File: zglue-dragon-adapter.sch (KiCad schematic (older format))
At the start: 56 parts, among them J1 543630489, J2 543630489, U1 zGlue-Dragon

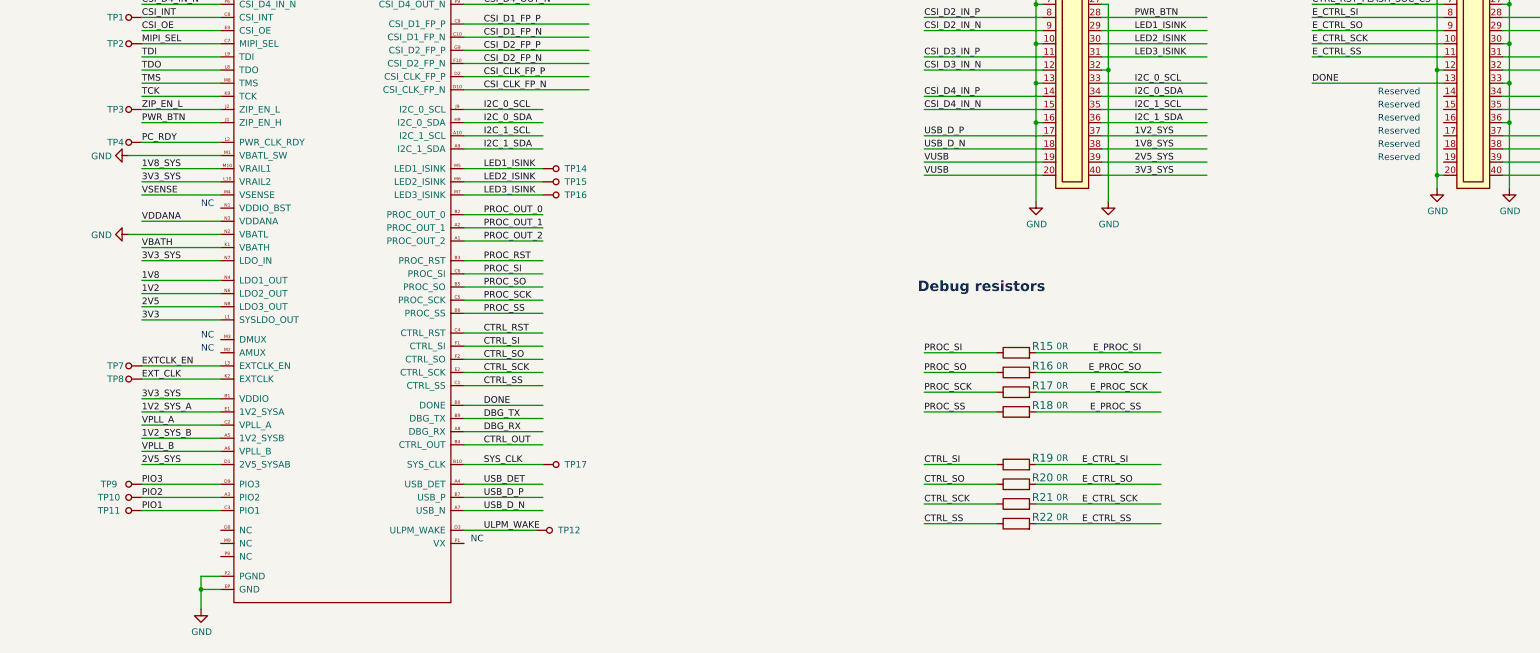
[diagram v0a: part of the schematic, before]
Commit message: Layout polishing, connected PROC_RST and CTRL_RST to chip via 0R
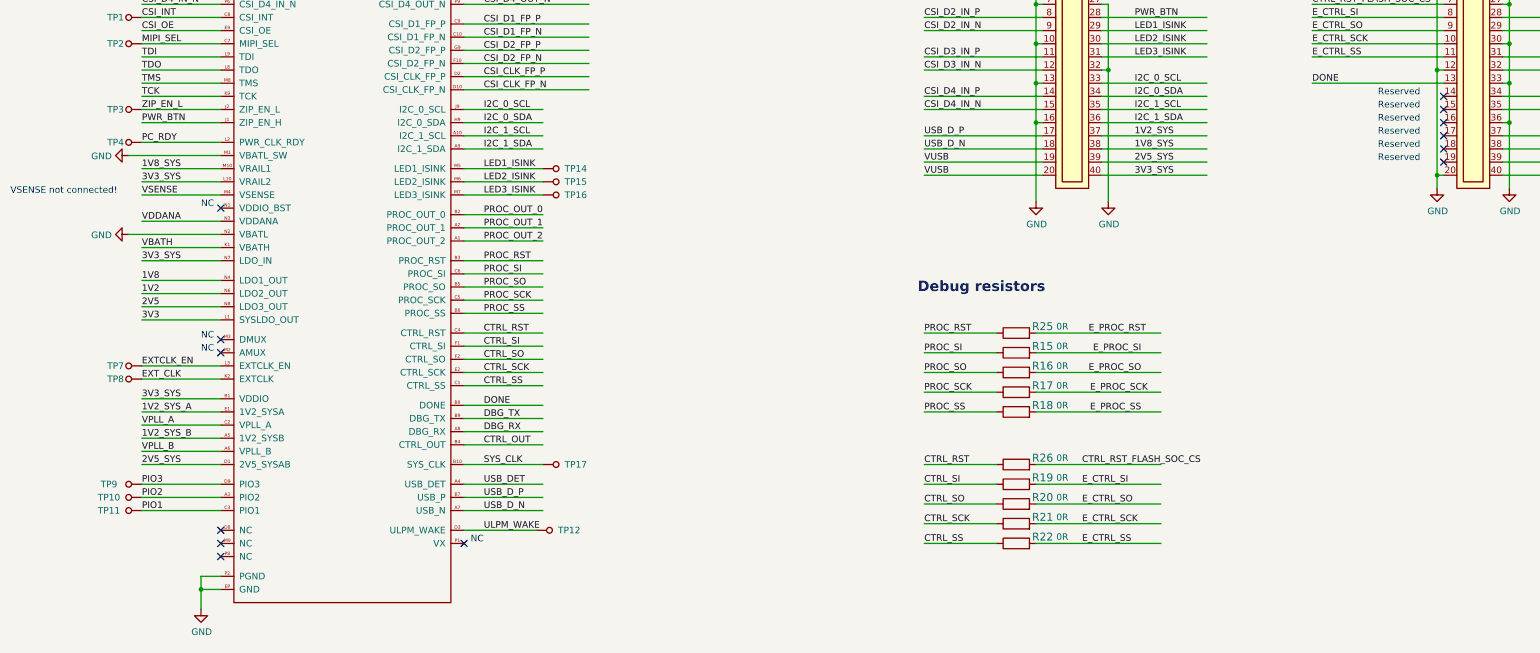
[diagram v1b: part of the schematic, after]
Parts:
- added R25, R26: R_0R_0402, antmicro-footprints:0402-res, symbol antmicroResistors0402:R_0R_0402
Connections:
- wire segments 259 -> 263
- no-connect marks 0 -> 13
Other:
- note added: "VSENSE not connected!"
- moved on the sheet: R19, R20, R21, R22
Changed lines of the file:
@@
 Text Label 10850 2150 0    50   ~ 0
 CTRL_RST_FLASH_SOC_CS
-Text Label 7900 5650 0    50   ~ 0
+Text Label 7900 5800 0    50   ~ 0
 CTRL_SI
-Text Label 7900 5800 0    50   ~ 0
+Text Label 7900 5950 0    50   ~ 0
 CTRL_SO
-Text Label 7900 5950 0    50   ~ 0
+Text Label 7900 6100 0    50   ~ 0
 CTRL_SCK
-Text Label 7900 6100 0    50   ~ 0
+Text Label 7900 6250 0    50   ~ 0
 CTRL_SS
 Text Label 9500 2050 0    50   ~ 0
@@
 L antmicroResistors0402:R_0R_0402 R19
 U 1 1 5E57F379
-P 8600 5650
-F 0 "R19" H 8800 5700 60  0000 C CNN
-F 1 "R_0R_0402" H 8600 5500 60  0001 C CNN
-F 2 "antmicro-footprints:0402-res" H 8800 5850 60  0001 L CNN
-F 3 "" H 8600 5650 50  0001 C CNN
-F 4 "PANASONIC" H 8800 6050 60  0001 L CNN "Manufacturer"
-F 5 "ERJ2GE0R00X" H 8800 5950 60  0001 L CNN "MPN"
-F 6 "0R" H 8950 5700 50  0000 C CNN "Val"
-	1    8600 5650
-	1    0    0    -1
-$EndComp
-Wire Wire Line
-	7900 5650 8450 5650
-$Comp
-L antmicroResistors0402:R_0R_0402 R20
-U 1 1 5E57F389
 P 8600 5800
-F 0 "R20" H 8800 5850 60  0000 C CNN
+F 0 "R19" H 8800 5850 60  0000 C CNN
 F 1 "R_0R_0402" H 8600 5650 60  0001 C CNN
 F 2 "antmicro-footprints:0402-res" H 8800 6000 60  0001 L CNN
@@
 	7900 5800 8450 5800
 $Comp
-L antmicroResistors0402:R_0R_0402 R21
-U 1 1 5E57F395
+L antmicroResistors0402:R_0R_0402 R20
+U 1 1 5E57F389
 P 8600 5950
-F 0 "R21" H 8800 6000 60  0000 C CNN
+F 0 "R20" H 8800 6000 60  0000 C CNN
 F 1 "R_0R_0402" H 8600 5800 60  0001 C CNN
 F 2 "antmicro-footprints:0402-res" H 8800 6150 60  0001 L CNN
@@
 	7900 5950 8450 5950
 $Comp
-L antmicroResistors0402:R_0R_0402 R22
-U 1 1 5E57F3A1
+L antmicroResistors0402:R_0R_0402 R21
+U 1 1 5E57F395
 P 8600 6100
-F 0 "R22" H 8800 6150 60  0000 C CNN
+F 0 "R21" H 8800 6150 60  0000 C CNN
 F 1 "R_0R_0402" H 8600 5950 60  0001 C CNN
 F 2 "antmicro-footprints:0402-res" H 8800 6300 60  0001 L CNN
@@
 Wire Wire Line
 	7900 6100 8450 6100
+$Comp
+L antmicroResistors0402:R_0R_0402 R22
+U 1 1 5E57F3A1
+P 8600 6250
+F 0 "R22" H 8800 6300 60  0000 C CNN
+F 1 "R_0R_0402" H 8600 6100 60  0001 C CNN
+F 2 "antmicro-footprints:0402-res" H 8800 6450 60  0001 L CNN
+F 3 "" H 8600 6250 50  0001 C CNN
+F 4 "PANASONIC" H 8800 6650 60  0001 L CNN "Manufacturer"
+F 5 "ERJ2GE0R00X" H 8800 6550 60  0001 L CNN "MPN"
+F 6 "0R" H 8950 6300 50  0000 C CNN "Val"
+	1    8600 6250
+	1    0    0    -1
+$EndComp
+Wire Wire Line
+	7900 6250 8450 6250
 Text Notes 7850 4350 0    79   ~ 16
 Debug resistors
@@
 Text Label 9550 5250 2    50   ~ 0
 E_PROC_SS
-Text Label 9100 5650 0    50   ~ 0
+Text Label 9100 5800 0    50   ~ 0
 E_CTRL_SI
-Text Label 9100 5800 0    50   ~ 0
+Text Label 9100 5950 0    50   ~ 0
 E_CTRL_SO
-Text Label 9100 5950 0    50   ~ 0
+Text Label 9100 6100 0    50   ~ 0
 E_CTRL_SCK
-Text Label 9100 6100 0    50   ~ 0
+Text Label 9100 6250 0    50   ~ 0
 E_CTRL_SS
 Wire Wire Line
@@
 	8750 5250 9700 5250
 Wire Wire Line
-	8750 5650 9700 5650
-Wire Wire Line
 	8750 5800 9700 5800
 Wire Wire Line
@@
 Wire Wire Line
 	8750 6100 9700 6100
+Wire Wire Line
+	8750 6250 9700 6250
 Text Label 1950 2450 0    50   ~ 0
 MIPI_SEL
@@
 Wire Wire Line
 	10900 8250 11650 8250
+NoConn ~ 2550 3700
+NoConn ~ 2550 4700
+NoConn ~ 2550 4800
+NoConn ~ 4400 6250
+NoConn ~ 11850 2850
+NoConn ~ 11850 2950
+NoConn ~ 11850 3050
+NoConn ~ 11850 3150
+NoConn ~ 11850 3250
+NoConn ~ 11850 3350
+NoConn ~ 2550 6150
+NoConn ~ 2550 6250
+NoConn ~ 2550 6350
+$Comp
+L antmicroResistors0402:R_0R_0402 R25
+U 1 1 5DC78E2D
+P 8600 4650
+F 0 "R25" H 8800 4700 60  0000 C CNN
+F 1 "R_0R_0402" H 8600 4500 60  0001 C CNN
+F 2 "antmicro-footprints:0402-res" H 8800 4850 60  0001 L CNN
+F 3 "" H 8600 4650 50  0001 C CNN
+F 4 "PANASONIC" H 8800 5050 60  0001 L CNN "Manufacturer"
+F 5 "ERJ2GE0R00X" H 8800 4950 60  0001 L CNN "MPN"
+F 6 "0R" H 8950 4700 50  0000 C CNN "Val"
+	1    8600 4650
+	1    0    0    -1
+$EndComp
+Wire Wire Line
+	8450 4650 7900 4650
+Wire Wire Line
+	8750 4650 9700 4650
+Text Label 7900 4650 0    50   ~ 0
+PROC_RST
+Text Label 9150 4650 0    50   ~ 0
+E_PROC_RST
+$Comp
+L antmicroResistors0402:R_0R_0402 R26
+U 1 1 5DCC1CB8
+P 8600 5650
+F 0 "R26" H 8800 5700 60  0000 C CNN
+F 1 "R_0R_0402" H 8600 5500 60  0001 C CNN
+F 2 "antmicro-footprints:0402-res" H 8800 5850 60  0001 L CNN
+F 3 "" H 8600 5650 50  0001 C CNN
+F 4 "PANASONIC" H 8800 6050 60  0001 L CNN "Manufacturer"
+F 5 "ERJ2GE0R00X" H 8800 5950 60  0001 L CNN "MPN"
+F 6 "0R" H 8950 5700 50  0000 C CNN "Val"
+	1    8600 5650
+	1    0    0    -1
+$EndComp
+Wire Wire Line
+	8450 5650 7900 5650
+Wire Wire Line
+	8750 5650 9700 5650
+Text Label 9100 5650 0    50   ~ 0
+CTRL_RST_FLASH_SOC_CS
+Text Label 7900 5650 0    50   ~ 0
+CTRL_RST
+Text Notes 950  3600 0    50   ~ 0
+VSENSE not connected!
 $EndSCHEMATC

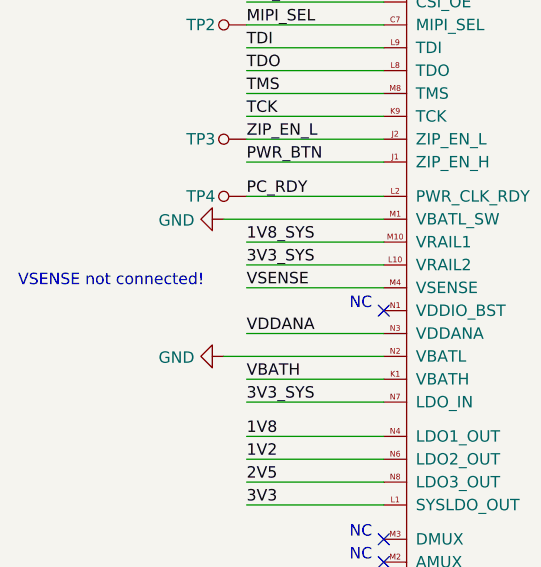
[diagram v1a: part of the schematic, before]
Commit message: Added testpad for VSENSE
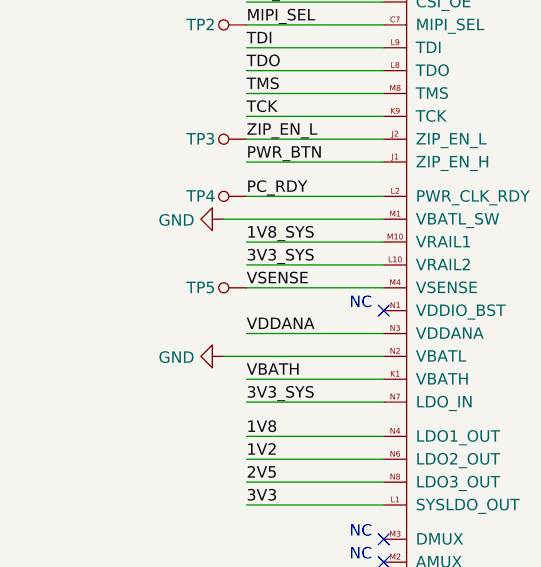
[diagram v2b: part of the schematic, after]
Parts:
- added TP5: TP_SMD1MM, antmicro-footprints:Testpoint_smd_1mm, symbol antmicroTestPoints:TP_SMD1MM
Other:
- note removed: "VSENSE not connected!"
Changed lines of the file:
@@
 Text Label 7900 5650 0    50   ~ 0
 CTRL_RST
-Text Notes 950  3600 0    50   ~ 0
-VSENSE not connected!
+$Comp
+L antmicroTestPoints:TP_SMD1MM TP5
+U 1 1 5DB1BFE4
+P 1850 3600
+F 0 "TP5" V 1850 3500 50  0000 C CNN
+F 1 "TP_SMD1MM" H 1850 3500 50  0001 C CNN
+F 2 "antmicro-footprints:Testpoint_smd_1mm" H 2050 3800 60  0001 L CNN
+F 3 "" H 2050 3900 60  0001 L CNN
+	1    1850 3600
+	0    1    1    0
+$EndComp
 $EndSCHEMATC

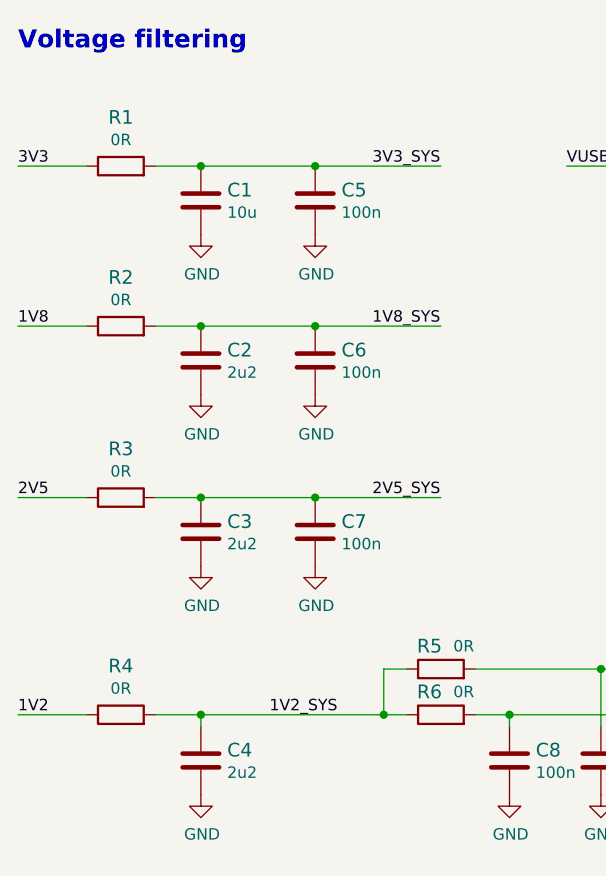
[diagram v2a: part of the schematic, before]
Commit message: Moved C1,2,3,4 closer to LDO output pins
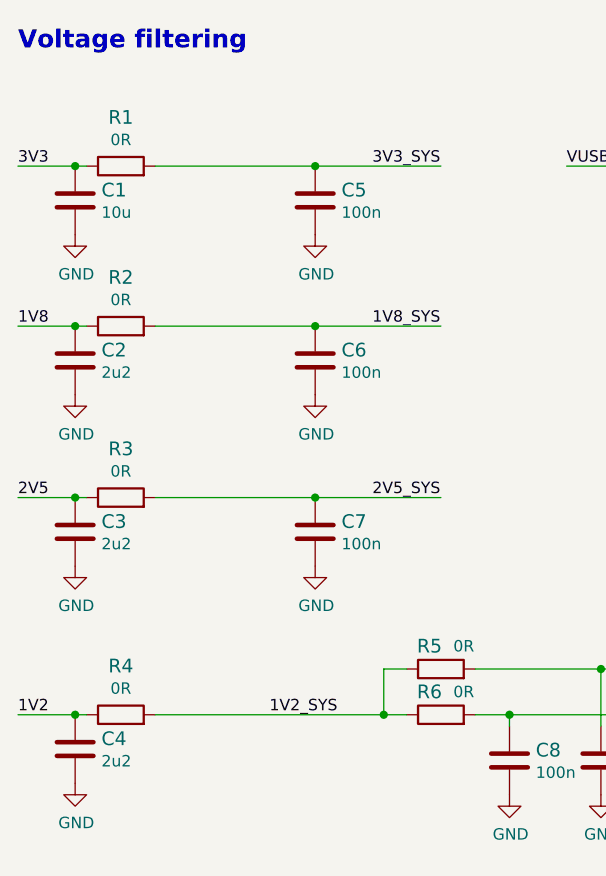
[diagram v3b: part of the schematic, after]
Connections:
- wire segments 263 -> 262
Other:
- moved on the sheet: C1, C2, C3, C4
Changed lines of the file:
@@
 L antmicroCapacitors0402:C_10u_0402 C1
 U 1 1 5DA0000B
-P 2000 8200
-F 0 "C1" H 2115 8245 60  0000 L CNN
-F 1 "C_10u_0402" H 2000 8050 60  0001 C CNN
-F 2 "antmicro-footprints:0402-cap" H 2200 8400 60  0001 L CNN
-F 3 "" H 2000 8200 50  0001 C CNN
-F 4 "TDK" H 2200 8600 60  0001 L CNN "Manufacturer"
-F 5 "C1005X5R0J106M050BC" H 2200 8500 60  0001 L CNN "MPN"
-F 6 "10u" H 2115 8147 50  0000 L CNN "Val"
-	1    2000 8200
+P 1450 8200
+F 0 "C1" H 1565 8245 60  0000 L CNN
+F 1 "C_10u_0402" H 1450 8050 60  0001 C CNN
+F 2 "antmicro-footprints:0402-cap" H 1650 8400 60  0001 L CNN
+F 3 "" H 1450 8200 50  0001 C CNN
+F 4 "TDK" H 1650 8600 60  0001 L CNN "Manufacturer"
+F 5 "C1005X5R0J106M050BC" H 1650 8500 60  0001 L CNN "MPN"
+F 6 "10u" H 1565 8147 50  0000 L CNN "Val"
+	1    1450 8200
 	1    0    0    -1
 $EndComp
@@
 L power:GND #PWR03
 U 1 1 5DA0044B
-P 2000 8350
-F 0 "#PWR03" H 2000 8100 50  0001 C CNN
-F 1 "GND" H 2005 8177 50  0000 C CNN
-F 2 "" H 2000 8350 50  0001 C CNN
-F 3 "" H 2000 8350 50  0001 C CNN
-	1    2000 8350
+P 1450 8350
+F 0 "#PWR03" H 1450 8100 50  0001 C CNN
+F 1 "GND" H 1455 8177 50  0000 C CNN
+F 2 "" H 1450 8350 50  0001 C CNN
+F 3 "" H 1450 8350 50  0001 C CNN
+	1    1450 8350
 	1    0    0    -1
 $EndComp
@@
 $EndComp
 Wire Wire Line
-	1800 8050 2000 8050
-Connection ~ 2000 8050
-Wire Wire Line
-	2000 8050 2500 8050
-Wire Wire Line
 	2500 8050 3050 8050
 Connection ~ 2500 8050
 Wire Wire Line
-	1500 8050 1200 8050
+	1500 8050 1450 8050
 Text Label 1200 8050 0    50   ~ 0
 3V3
@@
 L power:GND #PWR04
 U 1 1 5DA29CC6
-P 2000 9050
-F 0 "#PWR04" H 2000 8800 50  0001 C CNN
-F 1 "GND" H 2005 8877 50  0000 C CNN
-F 2 "" H 2000 9050 50  0001 C CNN
-F 3 "" H 2000 9050 50  0001 C CNN
-	1    2000 9050
+P 1450 9050
+F 0 "#PWR04" H 1450 8800 50  0001 C CNN
+F 1 "GND" H 1455 8877 50  0000 C CNN
+F 2 "" H 1450 9050 50  0001 C CNN
+F 3 "" H 1450 9050 50  0001 C CNN
+	1    1450 9050
 	1    0    0    -1
 $EndComp
@@
 Connection ~ 2500 8750
 Wire Wire Line
-	1500 8750 1200 8750
-Wire Wire Line
-	1800 8750 2000 8750
+	1500 8750 1450 8750
 $Comp
 L antmicroCapacitors0402:C_2u2_0402 C2
 U 1 1 5DA30683
-P 2000 8900
-F 0 "C2" H 2115 8945 60  0000 L CNN
-F 1 "C_2u2_0402" H 2000 8750 60  0001 C CNN
-F 2 "antmicro-footprints:0402-cap" H 2200 9100 60  0001 L CNN
-F 3 "" H 2000 8900 50  0001 C CNN
-F 4 "TDK" H 2200 9300 60  0001 L CNN "Manufacturer"
-F 5 "C1005X5R1A225K050BC" H 2200 9200 60  0001 L CNN "MPN"
-F 6 "2u2" H 2115 8847 50  0000 L CNN "Val"
-	1    2000 8900
-	1    0    0    -1
-$EndComp
-Connection ~ 2000 8750
-Wire Wire Line
-	2000 8750 2500 8750
+P 1450 8900
+F 0 "C2" H 1565 8945 60  0000 L CNN
+F 1 "C_2u2_0402" H 1450 8750 60  0001 C CNN
+F 2 "antmicro-footprints:0402-cap" H 1650 9100 60  0001 L CNN
+F 3 "" H 1450 8900 50  0001 C CNN
+F 4 "TDK" H 1650 9300 60  0001 L CNN "Manufacturer"
+F 5 "C1005X5R1A225K050BC" H 1650 9200 60  0001 L CNN "MPN"
+F 6 "2u2" H 1565 8847 50  0000 L CNN "Val"
+	1    1450 8900
+	1    0    0    -1
+$EndComp
 $Comp
 L antmicroCapacitors0402:C_100n_0402_6V3 C8
@@
 L power:GND #PWR06
 U 1 1 5DA307EF
-P 2000 10800
-F 0 "#PWR06" H 2000 10550 50  0001 C CNN
-F 1 "GND" H 2005 10627 50  0000 C CNN
-F 2 "" H 2000 10800 50  0001 C CNN
-F 3 "" H 2000 10800 50  0001 C CNN
-	1    2000 10800
+P 1450 10750
+F 0 "#PWR06" H 1450 10500 50  0001 C CNN
+F 1 "GND" H 1455 10577 50  0000 C CNN
+F 2 "" H 1450 10750 50  0001 C CNN
+F 3 "" H 1450 10750 50  0001 C CNN
+	1    1450 10750
 	1    0    0    -1
 $EndComp
@@
 $EndComp
 Wire Wire Line
-	1500 10450 1200 10450
-Wire Wire Line
-	1800 10450 2000 10450
-Connection ~ 2000 10450
+	1500 10450 1450 10450
 $Comp
 L antmicroCapacitors0402:C_2u2_0402 C4
 U 1 1 5DA3080C
-P 2000 10650
-F 0 "C4" H 2115 10695 60  0000 L CNN
-F 1 "C_2u2_0402" H 2000 10500 60  0001 C CNN
-F 2 "antmicro-footprints:0402-cap" H 2200 10850 60  0001 L CNN
-F 3 "" H 2000 10650 50  0001 C CNN
-F 4 "TDK" H 2200 11050 60  0001 L CNN "Manufacturer"
-F 5 "C1005X5R1A225K050BC" H 2200 10950 60  0001 L CNN "MPN"
-F 6 "2u2" H 2115 10597 50  0000 L CNN "Val"
-	1    2000 10650
+P 1450 10600
+F 0 "C4" H 1565 10645 60  0000 L CNN
+F 1 "C_2u2_0402" H 1450 10450 60  0001 C CNN
+F 2 "antmicro-footprints:0402-cap" H 1650 10800 60  0001 L CNN
+F 3 "" H 1450 10600 50  0001 C CNN
+F 4 "TDK" H 1650 11000 60  0001 L CNN "Manufacturer"
+F 5 "C1005X5R1A225K050BC" H 1650 10900 60  0001 L CNN "MPN"
+F 6 "2u2" H 1565 10547 50  0000 L CNN "Val"
+	1    1450 10600
 	1    0    0    -1
 $EndComp
@@
 Wire Wire Line
 	3200 10450 3350 10450
-Wire Wire Line
-	2000 10450 2800 10450
-Wire Wire Line
-	2000 10500 2000 10450
 $Comp
 L power:GND #PWR011
@@
 L power:GND #PWR05
 U 1 1 5DB84A7E
-P 2000 9800
-F 0 "#PWR05" H 2000 9550 50  0001 C CNN
-F 1 "GND" H 2005 9627 50  0000 C CNN
-F 2 "" H 2000 9800 50  0001 C CNN
-F 3 "" H 2000 9800 50  0001 C CNN
-	1    2000 9800
+P 1450 9800
+F 0 "#PWR05" H 1450 9550 50  0001 C CNN
+F 1 "GND" H 1455 9627 50  0000 C CNN
+F 2 "" H 1450 9800 50  0001 C CNN
+F 3 "" H 1450 9800 50  0001 C CNN
+	1    1450 9800
 	1    0    0    -1
 $EndComp
@@
 Connection ~ 2500 9500
 Wire Wire Line
-	1500 9500 1200 9500
-Wire Wire Line
-	1800 9500 2000 9500
+	1500 9500 1450 9500
 $Comp
 L antmicroCapacitors0402:C_2u2_0402 C3
 U 1 1 5DB84A9B
-P 2000 9650
-F 0 "C3" H 2115 9695 60  0000 L CNN
-F 1 "C_2u2_0402" H 2000 9500 60  0001 C CNN
-F 2 "antmicro-footprints:0402-cap" H 2200 9850 60  0001 L CNN
-F 3 "" H 2000 9650 50  0001 C CNN
-F 4 "TDK" H 2200 10050 60  0001 L CNN "Manufacturer"
-F 5 "C1005X5R1A225K050BC" H 2200 9950 60  0001 L CNN "MPN"
-F 6 "2u2" H 2115 9597 50  0000 L CNN "Val"
-	1    2000 9650
-	1    0    0    -1
-$EndComp
-Connection ~ 2000 9500
-Wire Wire Line
-	2000 9500 2500 9500
+P 1450 9650
+F 0 "C3" H 1565 9695 60  0000 L CNN
+F 1 "C_2u2_0402" H 1450 9500 60  0001 C CNN
+F 2 "antmicro-footprints:0402-cap" H 1650 9850 60  0001 L CNN
+F 3 "" H 1450 9650 50  0001 C CNN
+F 4 "TDK" H 1650 10050 60  0001 L CNN "Manufacturer"
+F 5 "C1005X5R1A225K050BC" H 1650 9950 60  0001 L CNN "MPN"
+F 6 "2u2" H 1565 9597 50  0000 L CNN "Val"
+	1    1450 9650
+	1    0    0    -1
+$EndComp
 Text Label 6350 8500 0    50   ~ 0
 CSI_OE
@@
 	0    1    1    0
 $EndComp
+Connection ~ 1450 8050
+Wire Wire Line
+	1450 8050 1200 8050
+Wire Wire Line
+	1800 8050 2500 8050
+Connection ~ 1450 8750
+Wire Wire Line
+	1450 8750 1200 8750
+Wire Wire Line
+	1800 8750 2500 8750
+Connection ~ 1450 9500
+Wire Wire Line
+	1450 9500 1200 9500
+Wire Wire Line
+	1800 9500 2500 9500
+Connection ~ 1450 10450
+Wire Wire Line
+	1450 10450 1200 10450
+Wire Wire Line
+	1800 10450 2800 10450
 $EndSCHEMATC

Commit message: Library cleanup
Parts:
- C1: footprint antmicro-footprints:0402-cap -> zglue-dragon-adapter-footprints:0402-cap; symbol antmicroCapacitors0402:C_10u_0402 -> zglue-dragon-adapter:C_10u_0402
- C10, C11, C12, C14, C5, C6, C7, C8, C9: footprint antmicro-footprints:0402-cap -> zglue-dragon-adapter-footprints:0402-cap; symbol antmicroCapacitors0402:C_100n_0402_6V3 -> zglue-dragon-adapter:C_100n_0402_6V3
- C13, C15: footprint antmicro-footprints:0402-cap -> zglue-dragon-adapter-footprints:0402-cap; symbol antmicroCapacitors0402:C_10n_0402 -> zglue-dragon-adapter:C_10n_0402
- C2, C3, C4: footprint antmicro-footprints:0402-cap -> zglue-dragon-adapter-footprints:0402-cap; symbol antmicroCapacitors0402:C_2u2_0402 -> zglue-dragon-adapter:C_2u2_0402
- J1, J2: footprint antmicro-footprints:543630489 -> zglue-dragon-adapter-footprints:543630489; symbol antmicroB2bConnectors:543630489 -> zglue-dragon-adapter:543630489; MPN (none) -> 543630489; Manufacturer (none) -> Molex
- R1, R15, R16, R17, R18, R19, R2, R20, R21, R22, R25, R26, R3, R4, R5, R6, R7, R8: footprint antmicro-footprints:0402-res -> zglue-dragon-adapter-footprints:0402-res; symbol antmicroResistors0402:R_0R_0402 -> zglue-dragon-adapter:R_0R_0402
- R10, R12, R14, R23, R9: footprint antmicro-footprints:0402-res -> zglue-dragon-adapter-footprints:0402-res; symbol antmicroResistors0402:R_100R_0402 -> zglue-dragon-adapter:R_100R_0402
- R11: footprint antmicro-footprints:0402-res -> zglue-dragon-adapter-footprints:0402-res; symbol antmicroResistors0402:R_1k5_0402 -> zglue-dragon-adapter:R_1k5_0402
- R13: footprint antmicro-footprints:0402-res -> zglue-dragon-adapter-footprints:0402-res; symbol antmicroResistors0402:R_10k_0402 -> zglue-dragon-adapter:R_10k_0402
- R24: footprint antmicro-footprints:0402-res -> zglue-dragon-adapter-footprints:0402-res; symbol antmicroResistors0402:R_220R_0402 -> zglue-dragon-adapter:R_220R_0402
- TP1, TP10, TP11, TP12, TP14, TP15, TP16, TP17, TP2, TP3, TP4, TP5, TP7, TP8, TP9: footprint antmicro-footprints:Testpoint_smd_1mm -> zglue-dragon-adapter-footprints:Testpoint_smd_1mm; symbol antmicroTestPoints:TP_SMD1MM -> zglue-dragon-adapter:TP_SMD1MM
- U1: footprint lib:Z-Glue_LGA-96 -> zglue-dragon-adapter-footprints:Z-Glue_LGA-96; symbol zglue-dragon:zGlue-Dragon -> zglue-dragon-adapter:zGlue-Dragon
